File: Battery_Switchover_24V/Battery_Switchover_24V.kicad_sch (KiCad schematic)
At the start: 0 parts

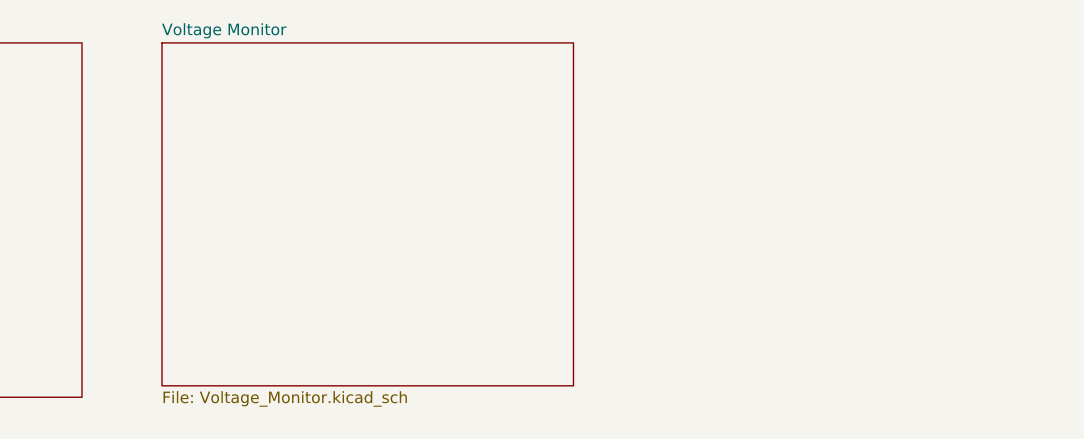
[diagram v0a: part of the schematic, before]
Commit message: Akım devresi eklendi Diğer devrelerde değişikler yapıldı
24 volttan tps54560 ile 5V oradan linear regulator ile 3.3V dönüştürüldü.

LPC11U14 e cristal eklendi
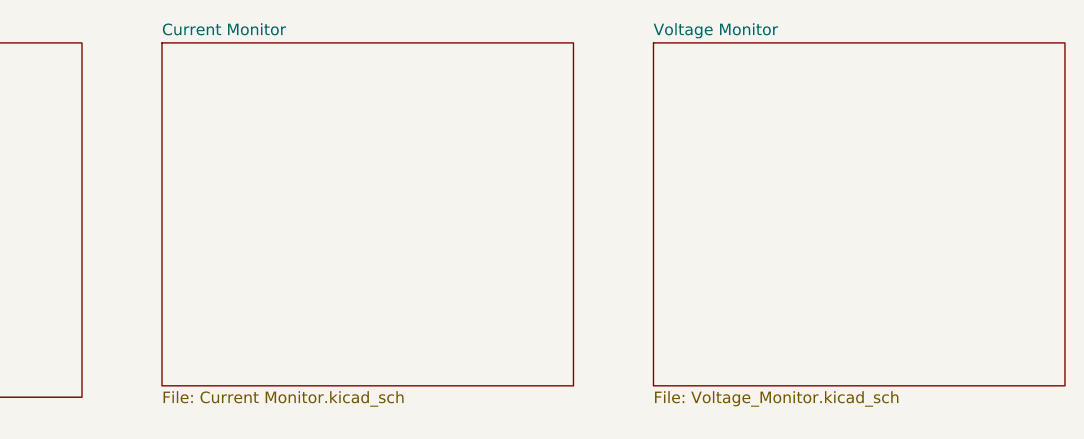
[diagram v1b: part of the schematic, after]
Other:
- added sheet Current Monitor (Current Monitor.kicad_sch)
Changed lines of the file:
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@@
 	(paper "A4")
+	(sheet
+		(at 139.7 34.29)
+		(size 45.72 38.1)
+		(exclude_from_sim no)
+		(in_bom yes)
+		(on_board yes)
+		(dnp no)
+		(fields_autoplaced yes)
+		(stroke
+			(width 0.1524)
+			(type solid)
+		)
+		(fill
+			(color 0 0 0 0.0000)
+		)
+		(property "Sheetname" "Voltage Monitor"
+			(at 139.7 33.5784 0)
+			(effects
+				(font
+					(size 1.27 1.27)
+				)
+				(justify left bottom)
+			)
+		)
+		(property "Sheetfile" "Voltage_Monitor.kicad_sch"
+			(at 139.7 72.9746 0)
+			(effects
+				(font
+					(size 1.27 1.27)
+				)
+				(justify left top)
+			)
+		)
+		(instances
+			(project "Battery_Switchover_24V"
+				(path "/045845e0-5d00-4da8-961e-99bdf190f683"
+					(page "3")
+				)
+			)
+		)
+	)
 	(sheet
 		(at 85.09 34.29)
@@
 			(color 0 0 0 0.0000)
 		)
-		(property "Sheetname" "Voltage Monitor"
+		(property "Sheetname" "Current Monitor"
 			(at 85.09 33.5784 0)
 			(effects
@@
 			)
 		)
-		(property "Sheetfile" "Voltage_Monitor.kicad_sch"
+		(property "Sheetfile" "Current Monitor.kicad_sch"
 			(at 85.09 72.9746 0)
 			(effects
@@
 			(project "Battery_Switchover_24V"
 				(path "/045845e0-5d00-4da8-961e-99bdf190f683"
-					(page "3")
+					(page "4")
 				)
 			)

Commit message: sch notes
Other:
- sheet Voltage Monitor renamed PowerSW
- sheet power_switch renamed CPU
- sheet CPU: file power_switch.kicad_sch -> cpu.kicad_sch
- sheet PowerSW: file Voltage_Monitor.kicad_sch -> powersw.kicad_sch
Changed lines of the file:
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@@
 			(color 0 0 0 0.0000)
 		)
-		(property "Sheetname" "Voltage Monitor"
-			(at 139.7 33.5784 0)
+		(property "Sheetname" "PowerSW"
+			(at 139.7 32.9434 0)
 			(effects
 				(font
-					(size 1.27 1.27)
+					(size 2.54 2.54)
 				)
 				(justify left bottom)
 			)
 		)
-		(property "Sheetfile" "Voltage_Monitor.kicad_sch"
+		(property "Sheetfile" "powersw.kicad_sch"
 			(at 139.7 72.9746 0)
 			(effects
@@
 		)
 		(property "Sheetname" "Current Monitor"
-			(at 85.09 33.5784 0)
+			(at 85.09 32.9434 0)
 			(effects
 				(font
-					(size 1.27 1.27)
+					(size 2.54 2.54)
 				)
 				(justify left bottom)
@@
 			(color 0 0 0 0.0000)
 		)
-		(property "Sheetname" "power_switch"
-			(at 30.48 33.5784 0)
+		(property "Sheetname" "CPU"
+			(at 30.48 32.9434 0)
 			(effects
 				(font
-					(size 1.27 1.27)
+					(size 2.54 2.54)
 				)
 				(justify left bottom)
 			)
 		)
-		(property "Sheetfile" "power_switch.kicad_sch"
+		(property "Sheetfile" "cpu.kicad_sch"
 			(at 30.48 74.2446 0)
 			(effects

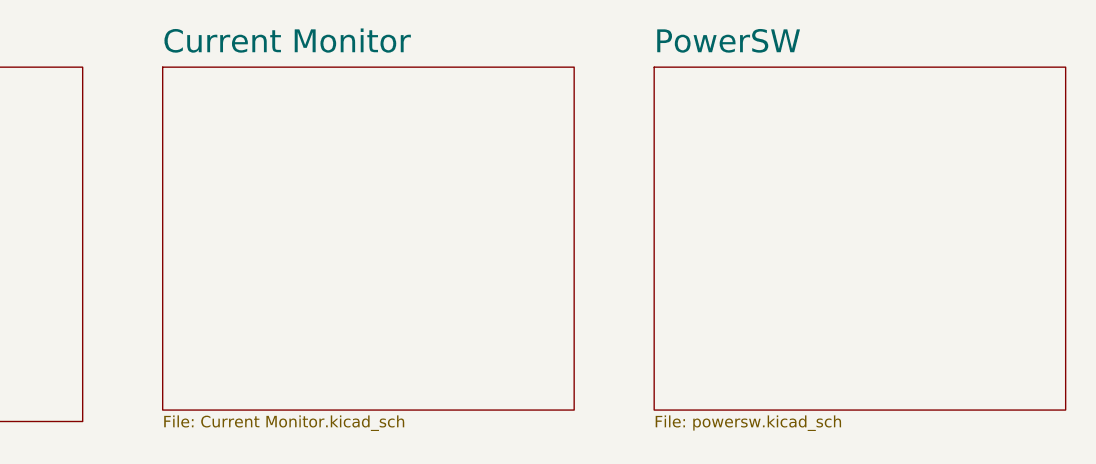
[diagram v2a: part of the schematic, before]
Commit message: General Improvements
Mosfet sayısı 1 e düştü polarize cap ler değiştirildi voltage converter değiştirildi
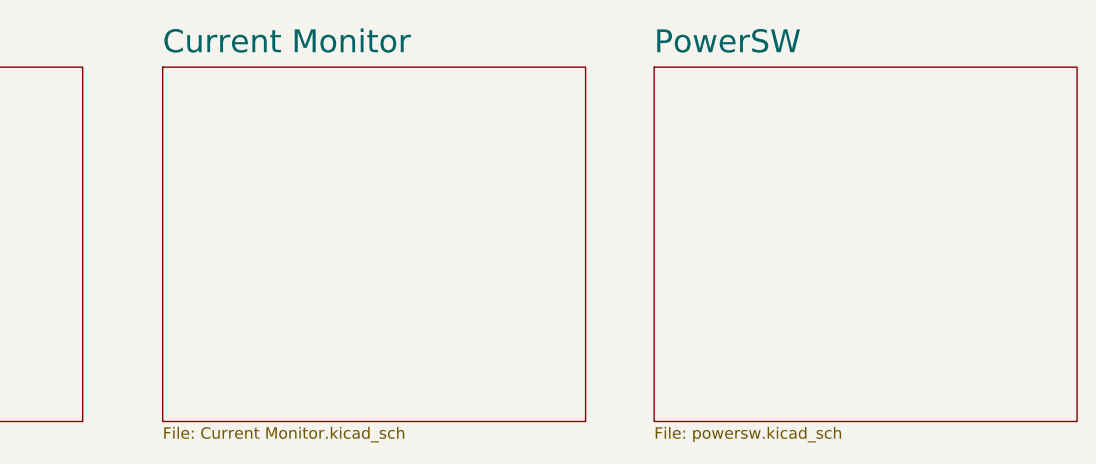
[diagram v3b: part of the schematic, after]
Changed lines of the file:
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@@
 	(sheet
 		(at 139.7 34.29)
-		(size 45.72 38.1)
+		(size 46.99 39.37)
 		(exclude_from_sim no)
 		(in_bom yes)
@@
 		)
 		(property "Sheetfile" "powersw.kicad_sch"
-			(at 139.7 72.9746 0)
+			(at 139.7 74.2446 0)
 			(effects
 				(font
@@
 	(sheet
 		(at 85.09 34.29)
-		(size 45.72 38.1)
+		(size 46.99 39.37)
 		(exclude_from_sim no)
 		(in_bom yes)
@@
 		)
 		(property "Sheetfile" "Current Monitor.kicad_sch"
-			(at 85.09 72.9746 0)
+			(at 85.09 74.2446 0)
 			(effects
 				(font

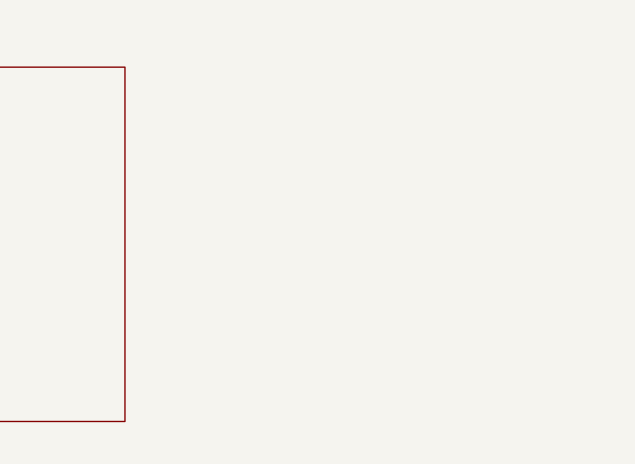
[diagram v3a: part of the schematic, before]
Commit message: Isı kontrollü eklendi bazı parçaların sembolleri değişti
Mosfetlere doğru semboller eklendi Isı kontorll IC eklendi Ledlerin bağlantıları yapıldı
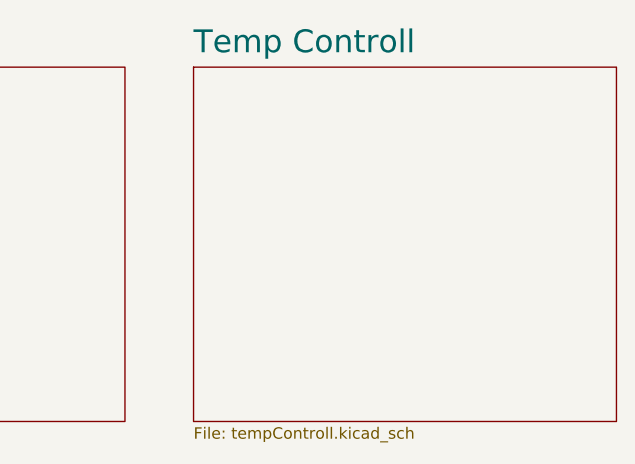
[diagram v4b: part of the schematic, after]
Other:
- added sheet Temp Controll (tempControll.kicad_sch)
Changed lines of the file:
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@@
+	)
+	(sheet
+		(at 194.31 34.29)
+		(size 46.99 39.37)
+		(exclude_from_sim no)
+		(in_bom yes)
+		(on_board yes)
+		(dnp no)
+		(fields_autoplaced yes)
+		(stroke
+			(width 0.1524)
+			(type solid)
+		)
+		(fill
+			(color 0 0 0 0.0000)
+		)
+		(property "Sheetname" "Temp Controll"
+			(at 194.31 32.9434 0)
+			(effects
+				(font
+					(size 2.54 2.54)
+				)
+				(justify left bottom)
+			)
+		)
+		(property "Sheetfile" "tempControll.kicad_sch"
+			(at 194.31 74.2446 0)
+			(effects
+				(font
+					(size 1.27 1.27)
+				)
+				(justify left top)
+			)
+		)
+		(instances
+			(project "Battery_Switchover_24V"
+				(path "/045845e0-5d00-4da8-961e-99bdf190f683"
+					(page "5")
+				)
+			)
+		)
 	)
 	(sheet

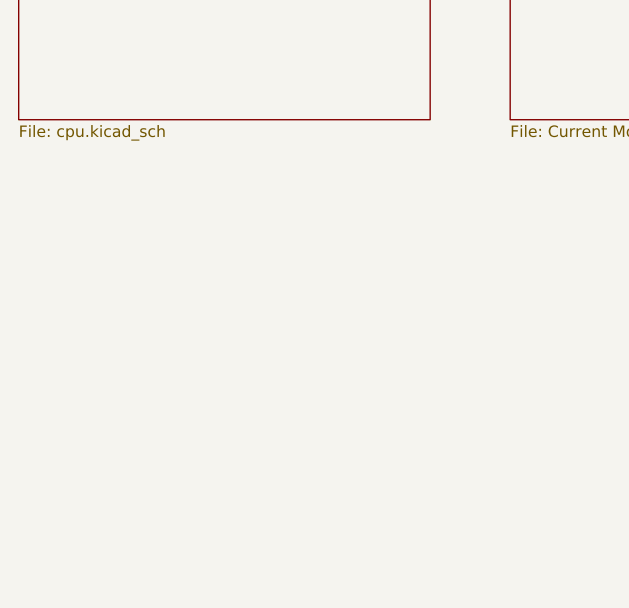
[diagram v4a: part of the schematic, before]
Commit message: Added Some Footprints
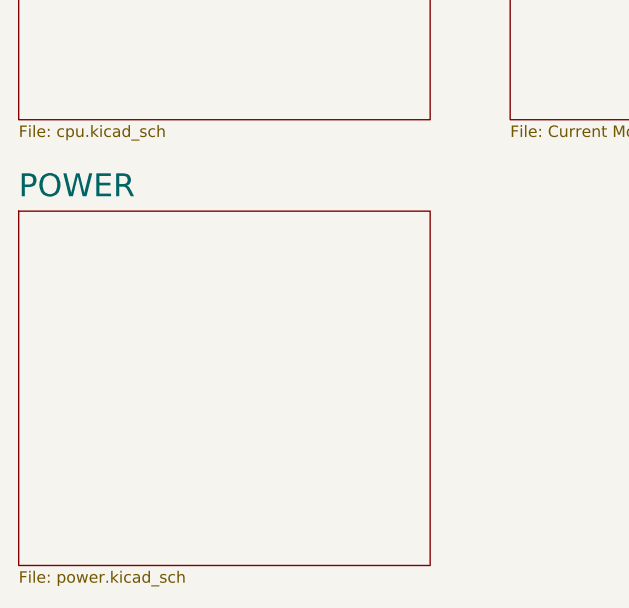
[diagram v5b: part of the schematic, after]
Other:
- added sheet POWER (power.kicad_sch)
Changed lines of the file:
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@@
 	(paper "A4")
+	(sheet
+		(at 30.48 83.82)
+		(size 45.72 39.37)
+		(exclude_from_sim no)
+		(in_bom yes)
+		(on_board yes)
+		(dnp no)
+		(fields_autoplaced yes)
+		(stroke
+			(width 0.1524)
+			(type solid)
+		)
+		(fill
+			(color 0 0 0 0.0000)
+		)
+		(property "Sheetname" "POWER"
+			(at 30.48 82.4734 0)
+			(effects
+				(font
+					(size 2.54 2.54)
+				)
+				(justify left bottom)
+			)
+		)
+		(property "Sheetfile" "power.kicad_sch"
+			(at 30.48 123.7746 0)
+			(effects
+				(font
+					(size 1.27 1.27)
+				)
+				(justify left top)
+			)
+		)
+		(instances
+			(project "Battery_Switchover_24V"
+				(path "/045845e0-5d00-4da8-961e-99bdf190f683"
+					(page "6")
+				)
+			)
+		)
+	)
 	(sheet
 		(at 139.7 34.29)

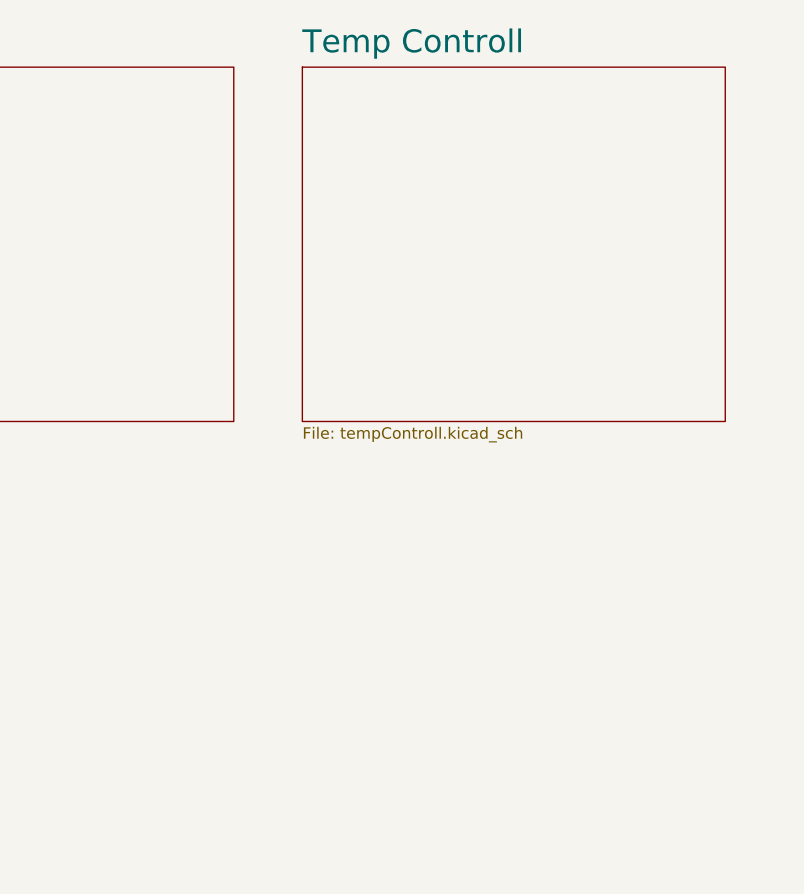
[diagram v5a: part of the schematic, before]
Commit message: Added board edge to PCB and some general placement as well as some schematic changes
Added connectors for Vin and for low side current monitoring(3 connectors) (connector types must be changed. Changes to the power controll circuit added bypass capacitor to the opamp. Added output connector
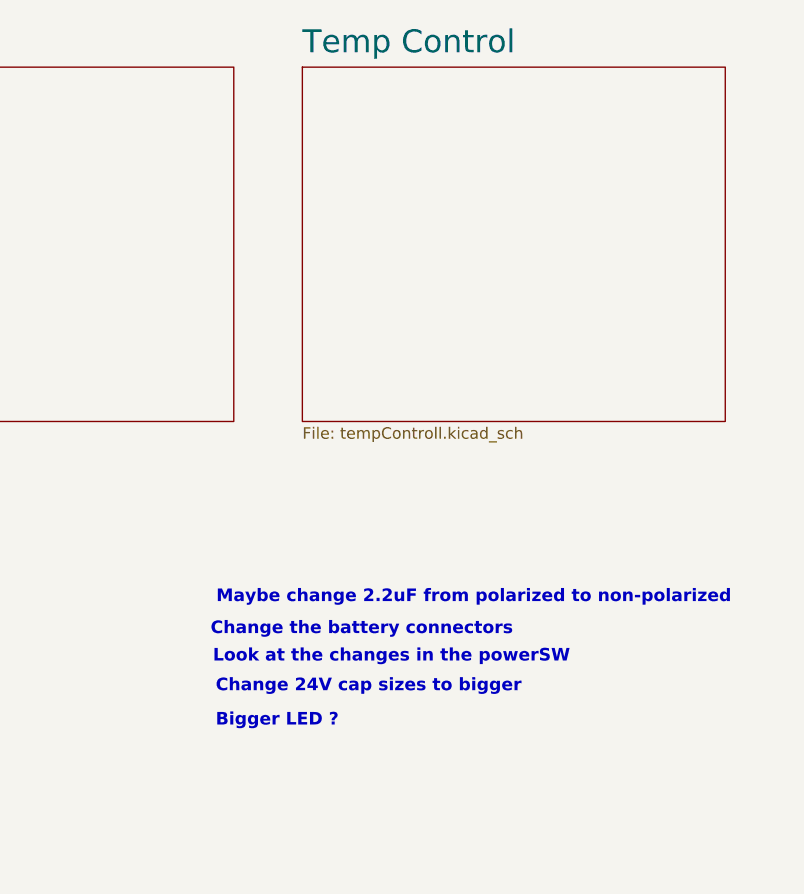
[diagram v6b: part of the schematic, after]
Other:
- sheet Temp Controll renamed Temp Control
- note added: "Bigger LED ?"
- note added: "Change 24V cap sizes to bigger"
- note added: "Change the battery connectors"
- note added: "Look at the changes in the powerSW"
- note added: "Maybe change 2.2uF from polarized to non-polarized"
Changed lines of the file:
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@@
 	(generator_version "9.0")
 	(paper "A4")
+	(text "Maybe change 2.2uF from polarized to non-polarized"
+		(exclude_from_sim no)
+		(at 213.36 93.218 0)
+		(effects
+			(font
+				(size 1.397 1.397)
+				(thickness 0.2794)
+				(bold yes)
+			)
+		)
+	)
+	(text "Change 24V cap sizes to bigger\n"
+		(exclude_from_sim no)
+		(at 201.676 103.124 0)
+		(effects
+			(font
+				(size 1.397 1.397)
+				(thickness 0.254)
+				(bold yes)
+			)
+		)
+	)
+	(text "Change the battery connectors"
+		(exclude_from_sim no)
+		(at 200.914 96.774 0)
+		(effects
+			(font
+				(size 1.397 1.397)
+				(thickness 0.2794)
+				(bold yes)
+			)
+		)
+	)
+	(text "Look at the changes in the powerSW"
+		(exclude_from_sim no)
+		(at 204.216 99.822 0)
+		(effects
+			(font
+				(size 1.397 1.397)
+				(thickness 0.254)
+				(bold yes)
+			)
+		)
+	)
+	(text "Bigger LED ?"
+		(exclude_from_sim no)
+		(at 191.516 106.934 0)
+		(effects
+			(font
+				(size 1.397 1.397)
+				(thickness 0.254)
+				(bold yes)
+			)
+		)
+	)
 	(sheet
 		(at 30.48 83.82)
@@
 			(color 0 0 0 0.0000)
 		)
-		(property "Sheetname" "Temp Controll"
+		(property "Sheetname" "Temp Control"
 			(at 194.31 32.9434 0)
 			(effects

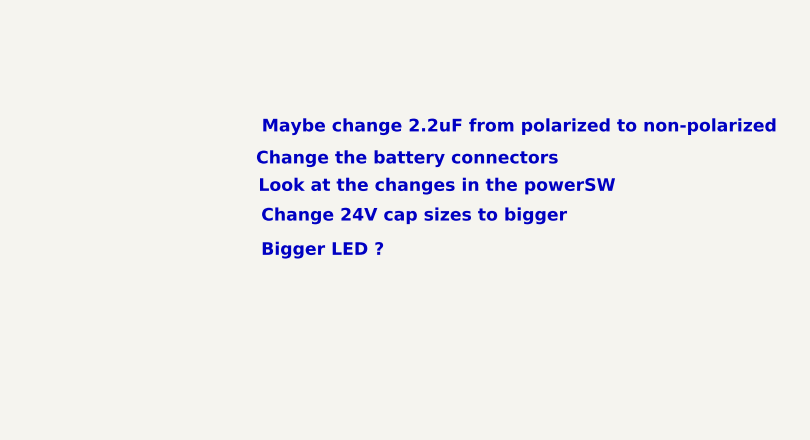
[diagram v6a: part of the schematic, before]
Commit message: Fixed opamp footprint issue done some preliminary placement
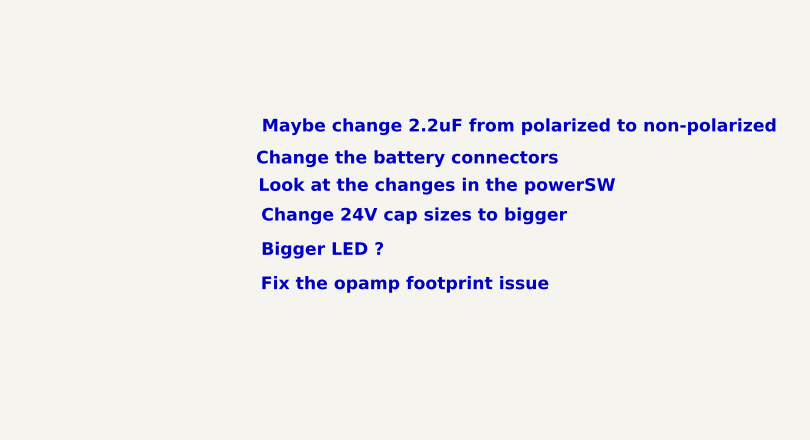
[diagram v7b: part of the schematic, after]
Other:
- note added: "Fix the opamp footprint issue"
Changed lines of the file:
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@@
 	(generator_version "9.0")
 	(paper "A4")
+	(text "Fix the opamp footprint issue"
+		(exclude_from_sim no)
+		(at 200.66 110.744 0)
+		(effects
+			(font
+				(size 1.397 1.397)
+				(thickness 0.2794)
+				(bold yes)
+			)
+		)
+	)
 	(text "Maybe change 2.2uF from polarized to non-polarized"
 		(exclude_from_sim no)

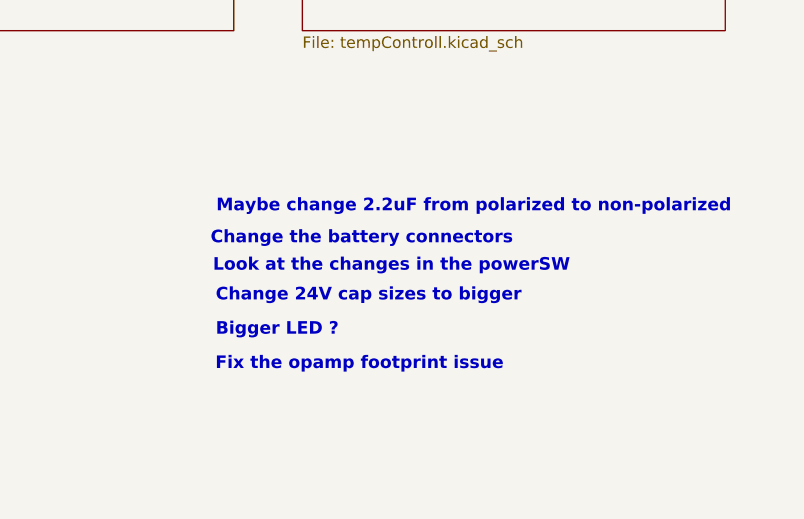
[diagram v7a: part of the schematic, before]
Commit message: Placement changes to shrink the board size
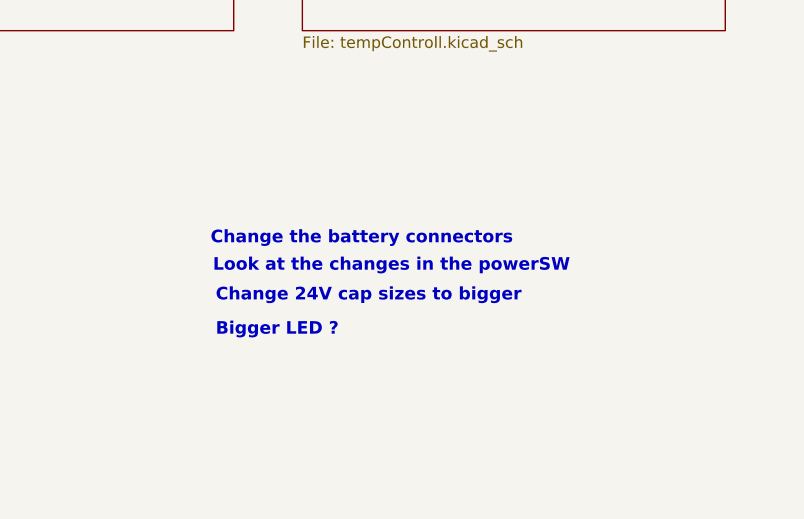
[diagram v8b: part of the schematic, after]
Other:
- note removed: "Fix the opamp footprint issue"
- note removed: "Maybe change 2.2uF from polarized to non-polarized"
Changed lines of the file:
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@@
 	(generator_version "9.0")
 	(paper "A4")
-	(text "Fix the opamp footprint issue"
-		(exclude_from_sim no)
-		(at 200.66 110.744 0)
-		(effects
-			(font
-				(size 1.397 1.397)
-				(thickness 0.2794)
-				(bold yes)
-			)
-		)
-	)
-	(text "Maybe change 2.2uF from polarized to non-polarized"
-		(exclude_from_sim no)
-		(at 213.36 93.218 0)
-		(effects
-			(font
-				(size 1.397 1.397)
-				(thickness 0.2794)
-				(bold yes)
-			)
-		)
-	)
 	(text "Change 24V cap sizes to bigger\n"
 		(exclude_from_sim no)
